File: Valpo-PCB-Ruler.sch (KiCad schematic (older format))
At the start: 2 parts, among them U1 ATtiny85-20PU

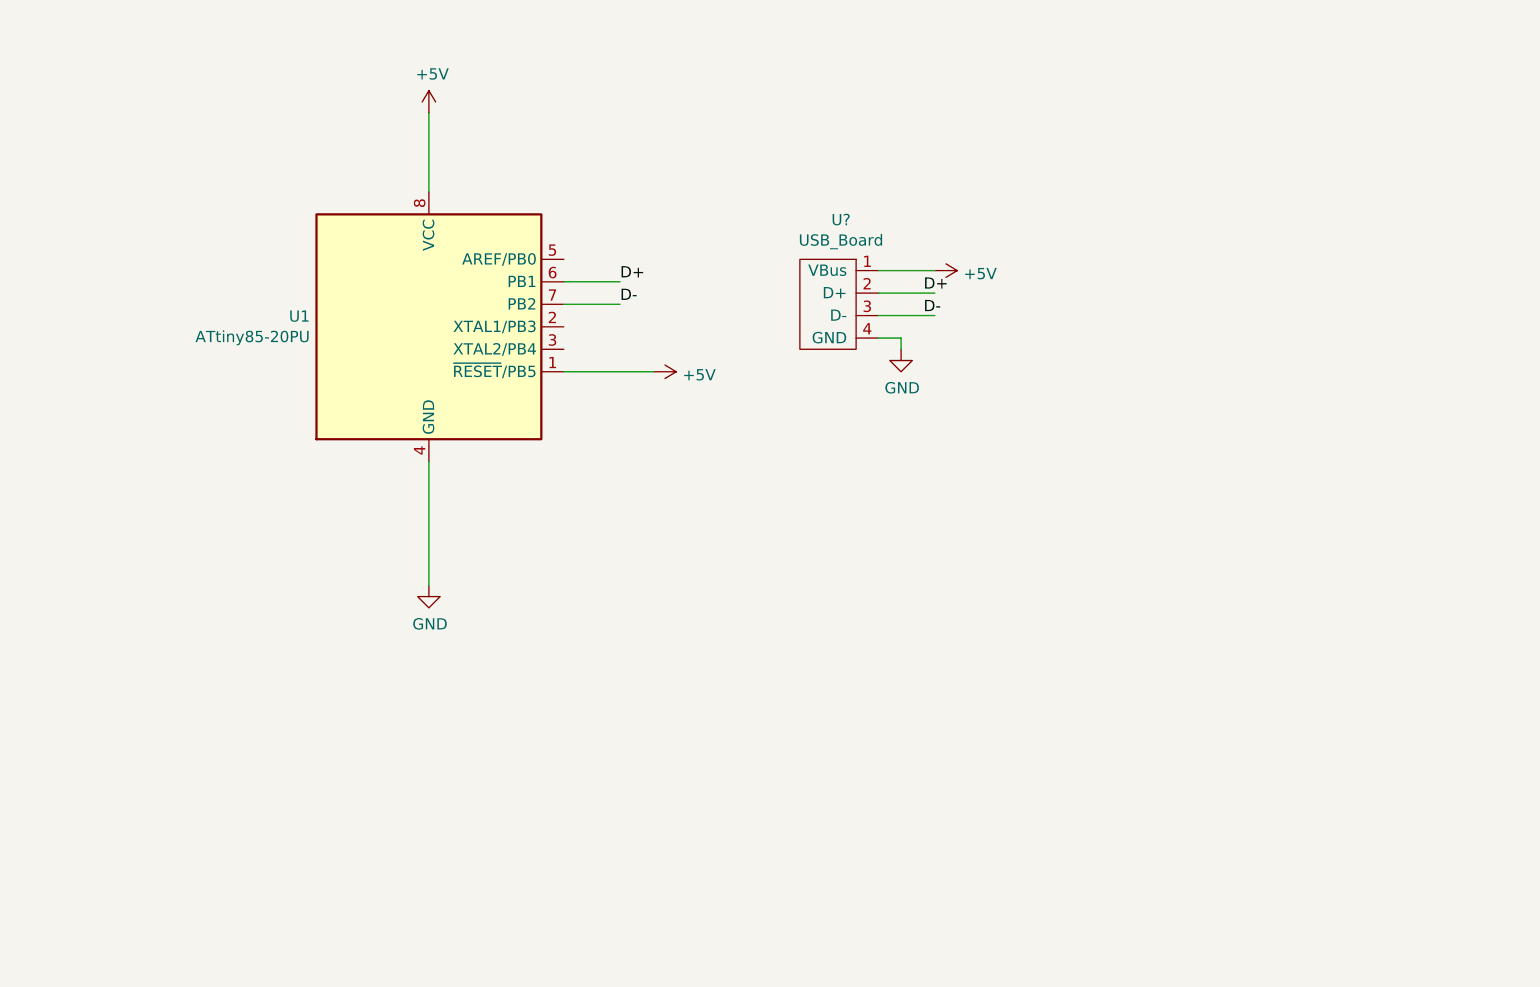
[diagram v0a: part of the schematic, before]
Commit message: Layout Set
Set out layout and schematics for both LCD and push-buttons. Users will have the option to use either or depending on which solder bridges they connect. Board USB also added to the device, may need to change which side of the board the traces are on if buttons/LCD are not visible.
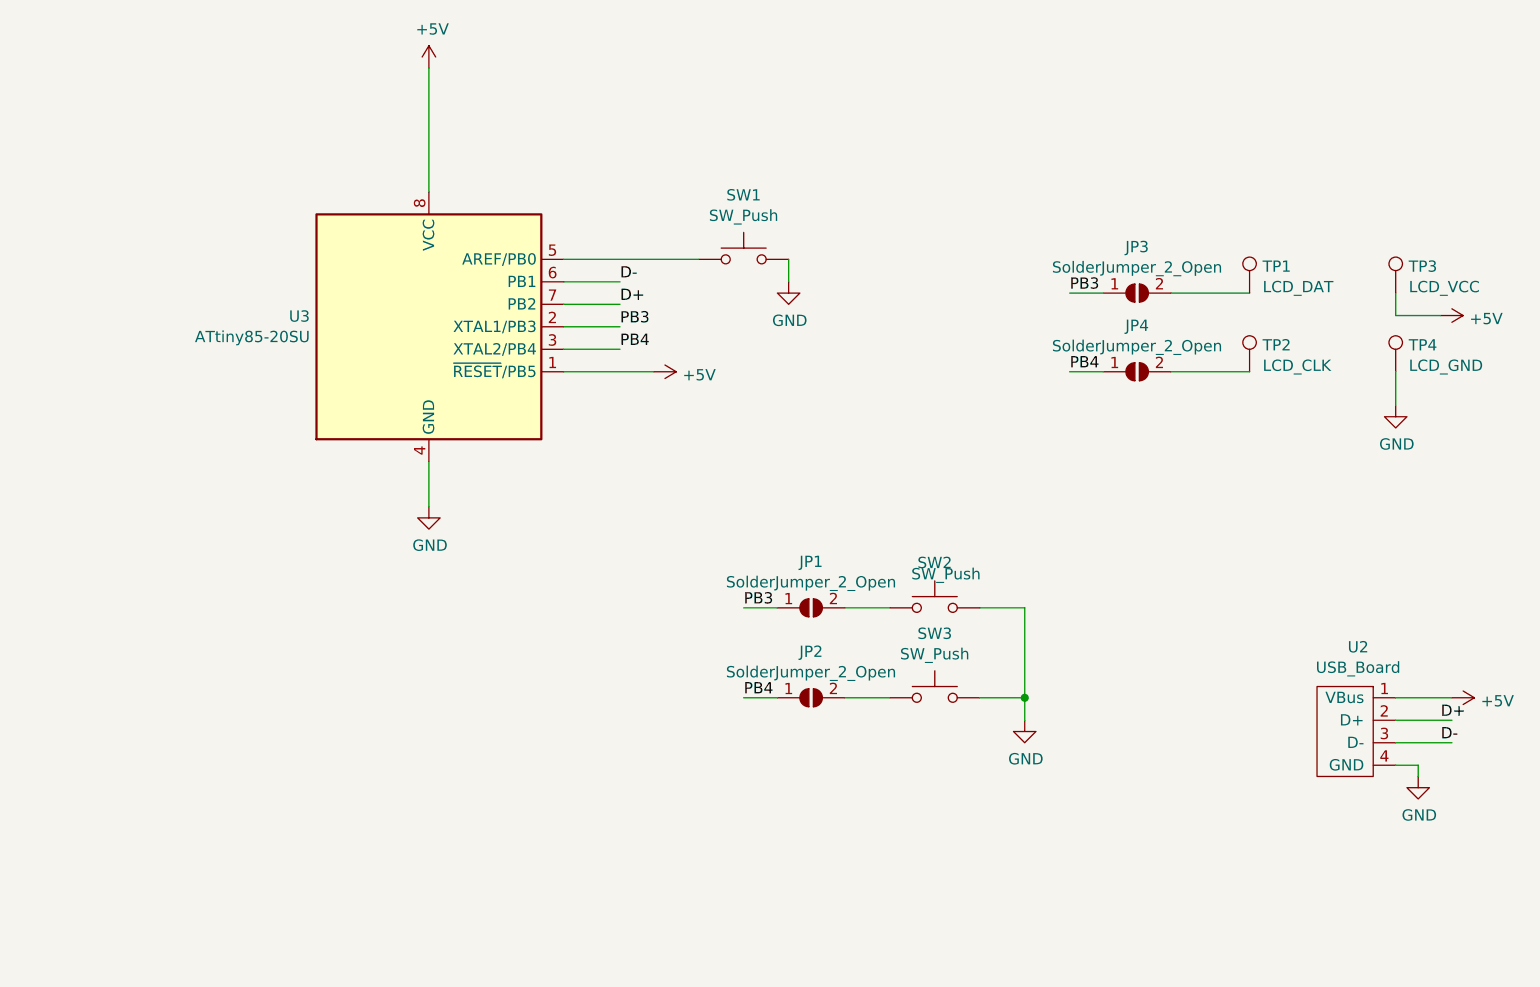
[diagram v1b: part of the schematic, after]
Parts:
- removed U1: ATtiny85-20PU, Package_DIP:DIP-8_W7.62mm, symbol MCU_Microchip_ATtiny:ATtiny85-20PU
- added JP1, JP2, JP3, JP4: SolderJumper_2_Open, Jumper:SolderJumper-2_P1.3mm_Open_Pad1.0x1.5mm, symbol Jumper:SolderJumper_2_Open
- added SW1, SW2, SW3: SW_Push, Button_Switch_SMD:SW_Push_SPST_NO_Alps_SKRK, symbol Switch:SW_Push
- added TP1: LCD_DAT, TestPoint:TestPoint_Pad_D1.0mm, symbol Connector:TestPoint
- added TP2: LCD_CLK, TestPoint:TestPoint_Pad_D1.0mm, symbol Connector:TestPoint
- added TP3: LCD_VCC, TestPoint:TestPoint_Pad_D1.0mm, symbol Connector:TestPoint
- added TP4: LCD_GND, TestPoint:TestPoint_Pad_1.0x1.0mm, symbol Connector:TestPoint
- added U3: ATtiny85-20SU, Package_SO:SOIJ-8_5.3x5.3mm_P1.27mm, symbol MCU_Microchip_ATtiny:ATtiny85-20SU
- gave numbers to parts that had none: 1
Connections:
- net labels added: PB3, PB4
- wire segments 10 -> 29
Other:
- moved on the sheet: U2

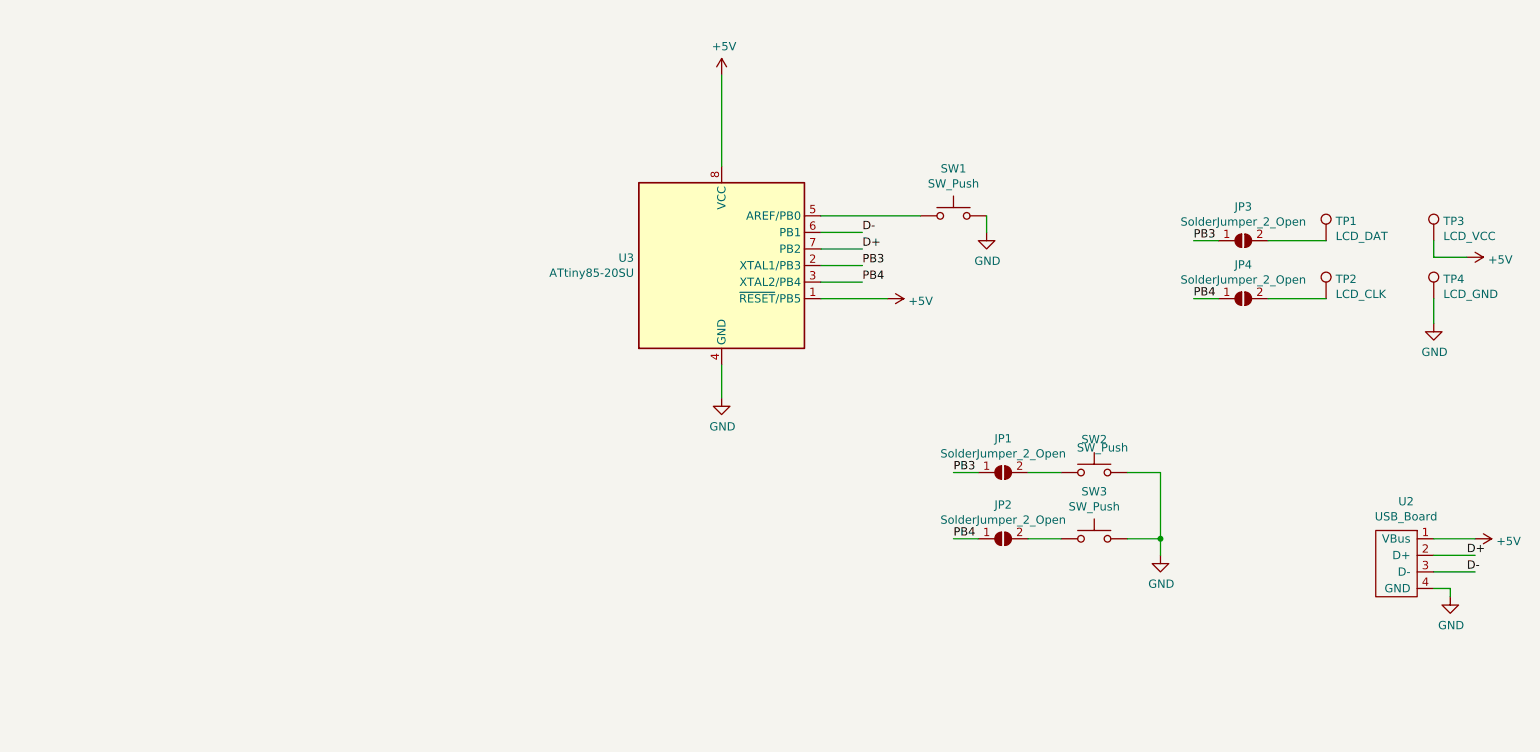
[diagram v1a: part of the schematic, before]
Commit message: Reverse USB side
Moved the USB to be on the other side of the board to maintain the sanctity of the zero on the left side (for the imperial units).
Reduced transistor diagrams to not some of the smaller diagrams. Added additional hardware to allow the ATtiny to work with USB.
Added some Mechanical engineering focused constants (Avogadro's Number, Gas Constant, Accl due to gravity in metric & imperial)
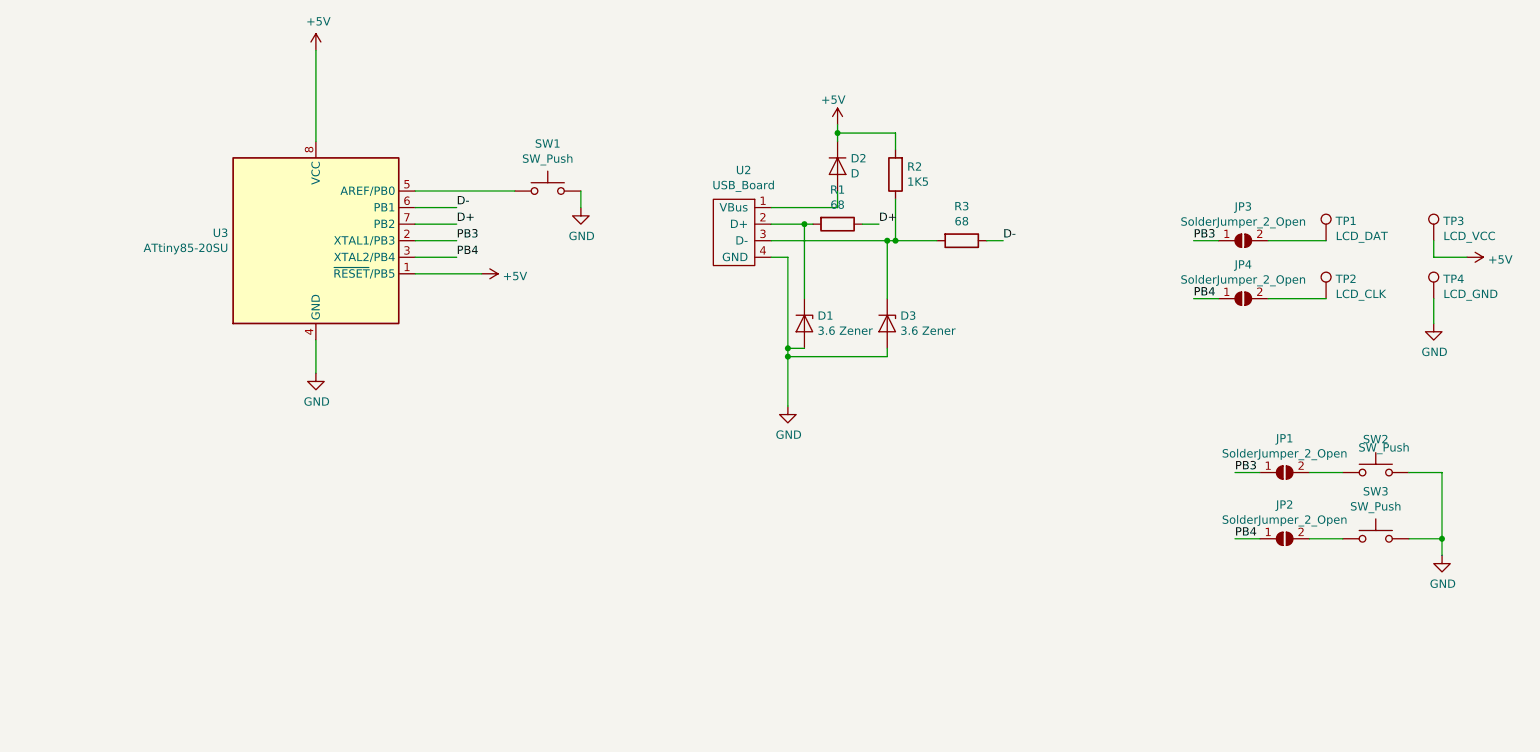
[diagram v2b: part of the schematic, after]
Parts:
- added D1, D3: 3.6 Zener, Diode_SMD:D_0402_1005Metric, symbol Device:D_Zener
- added D2: D, Diode_SMD:D_0402_1005Metric, symbol Device:D
- added R1, R3: 68, Resistor_SMD:R_0402_1005Metric, symbol Device:R
- added R2: 1K5, Resistor_SMD:R_0402_1005Metric, symbol Device:R
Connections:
- wire segments 29 -> 47
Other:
- moved on the sheet: JP1, JP2, SW1, SW2, SW3, U2, U3
